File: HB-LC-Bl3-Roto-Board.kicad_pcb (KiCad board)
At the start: 2 copper layers, 43 parts, among them IC1 ArduinoProMini, J1 Taster Verdunklung, J2 Taster Fenster, J3 Taster Sonnenschutz, J4 230V, J5 24V, J6 Motor Fenster 24V, J7 Motor Sonnenschutz 230V, J8 Motor Verdunklung 24V, K1 G6S-2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

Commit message: Intermediate commit
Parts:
- moved RL2 37.3 mm to (91.3, 87.7), turned to 270 degrees
- moved RL4 1.28 mm to (63.9, 117.7)
- moved F1 0.76 mm to (100.5, 117.4)
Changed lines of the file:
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@@
   )
   (module relay:FIN4061 (layer F.Cu)
-    (at 62.75 117.05)
+    (at 63.85 117.7)
     (fp_text reference RL4 (at 4.9 2.3) (layer F.SilkS)
       (effects (font (size 1 1) (thickness 0.15)))
@@
   )
   (module relay:FIN4061 (layer F.Cu)
-    (at 57.85 104.05)
-    (fp_text reference RL2 (at 4.9 2.3) (layer F.SilkS)
+    (at 91.35 87.65 270)
+    (fp_text reference RL2 (at 4.9 2.3 90) (layer F.SilkS)
       (effects (font (size 1 1) (thickness 0.15)))
     )
-    (fp_text value FINDER-40.61 (at 7.9 4.2) (layer F.Fab)
+    (fp_text value FINDER-40.61 (at 7.9 4.2 90) (layer F.Fab)
       (effects (font (size 1 1) (thickness 0.15)))
     )
@@
     (fp_line (start 26 10) (end -3 10) (layer F.SilkS) (width 0.15))
     (fp_line (start -3 -2.5) (end 26 -2.5) (layer F.SilkS) (width 0.15))
-    (pad A1 thru_hole circle (at 0 0) (size 3 3) (drill 1.5) (layers *.Cu *.Mask)
+    (pad A1 thru_hole circle (at 0 0 270) (size 3 3) (drill 1.5) (layers *.Cu *.Mask)
       (net 4 +24V))
-    (pad A2 thru_hole circle (at 0 7.5) (size 3 3) (drill 1.5) (layers *.Cu *.Mask)
+    (pad A2 thru_hole circle (at 0 7.5 270) (size 3 3) (drill 1.5) (layers *.Cu *.Mask)
       (net 6 "Net-(D3-Pad2)"))
-    (pad 11 thru_hole rect (at 20 0) (size 2.5 4) (drill 1.5) (layers *.Cu *.Mask)
+    (pad 11 thru_hole rect (at 20 0 270) (size 2.5 4) (drill 1.5) (layers *.Cu *.Mask)
       (net 52 /L_FUSED))
-    (pad 14 thru_hole rect (at 25 0) (size 2.5 4) (drill 1.5) (layers *.Cu *.Mask)
+    (pad 14 thru_hole rect (at 25 0 270) (size 2.5 4) (drill 1.5) (layers *.Cu *.Mask)
       (net 49 /M2_L))
-    (pad 12 thru_hole rect (at 15 0) (size 2.5 4) (drill 1.5) (layers *.Cu *.Mask)
+    (pad 12 thru_hole rect (at 15 0 270) (size 2.5 4) (drill 1.5) (layers *.Cu *.Mask)
       (net 50 "Net-(RL2-Pad12)"))
-    (pad 22 thru_hole rect (at 15 7.5) (size 2.5 4) (drill 1.5) (layers *.Cu *.Mask)
+    (pad 22 thru_hole rect (at 15 7.5 270) (size 2.5 4) (drill 1.5) (layers *.Cu *.Mask)
       (net 50 "Net-(RL2-Pad12)"))
-    (pad 21 thru_hole rect (at 20 7.5) (size 2.5 4) (drill 1.5) (layers *.Cu *.Mask)
+    (pad 21 thru_hole rect (at 20 7.5 270) (size 2.5 4) (drill 1.5) (layers *.Cu *.Mask)
       (net 52 /L_FUSED))
-    (pad 24 thru_hole rect (at 25 7.5) (size 2.5 4) (drill 1.5) (layers *.Cu *.Mask)
+    (pad 24 thru_hole rect (at 25 7.5 270) (size 2.5 4) (drill 1.5) (layers *.Cu *.Mask)
       (net 49 /M2_L))
   )
@@
   )
   (module Fuse:Fuseholder_Cylinder-5x20mm_Schurter_FPG4_Vertical_Closed (layer F.Cu)
-    (at 100.15 118.1 270)
+    (at 100.45 117.4 270)
     (descr "Shock-Safe Fuseholder, 5 x 20 mm, Slotted Cap/Fingergrip, vertical, IEC 60335-1; 250VAC/10A VDE; 500V/16A UL/CSA (https://us.schurter.com/bundles/snceschurter/epim/_ProdPool_/newDS/en/typ_FPG4.pdf)")
     (tags "fuse holder vertical 5x20mm")

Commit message: Version 1
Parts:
- added C10: 100n, Capacitor_THT:C_Rect_L4.6mm_W3.0mm_P2.50mm_MKS02_FKP02, F.Cu at (92.8, 113.4)
- added C7: 100n, Capacitor_THT:C_Rect_L4.6mm_W3.0mm_P2.50mm_MKS02_FKP02, F.Cu at (104.2, 113.6)
- added C8: 100n, Capacitor_THT:C_Rect_L4.6mm_W3.0mm_P2.50mm_MKS02_FKP02, F.Cu at (115.6, 113.6)
- added C9: 100n, Capacitor_THT:C_Rect_L4.6mm_W3.0mm_P2.50mm_MKS02_FKP02, F.Cu at (100.6, 113.4)
- added H1: MountingHole, MountingHole:MountingHole_3.2mm_M3, F.Cu at (79.2, 132.0)
- added H2: MountingHole, MountingHole:MountingHole_3.2mm_M3, F.Cu at (121.2, 85.6)
- added H3: MountingHole, MountingHole:MountingHole_3.2mm_M3, F.Cu at (29.8, 87.2)
- added R10: 47, Resistor_THT:R_Axial_DIN0204_L3.6mm_D1.6mm_P5.08mm_Horizontal, F.Cu at (123.6, 116.4)
- added R11: 10k, Resistor_THT:R_Axial_DIN0204_L3.6mm_D1.6mm_P5.08mm_Horizontal, F.Cu at (106.6, 116.4)
- added R12: 10k, Resistor_THT:R_Axial_DIN0204_L3.6mm_D1.6mm_P5.08mm_Horizontal, F.Cu at (118.0, 116.4)
- added R13: 47, Resistor_THT:R_Axial_DIN0204_L3.6mm_D1.6mm_P5.08mm_Horizontal, F.Cu at (104.0, 116.4)
- added R14: 47, Resistor_THT:R_Axial_DIN0204_L3.6mm_D1.6mm_P5.08mm_Horizontal, F.Cu at (115.4, 116.4)
- added R15: 10k, Resistor_THT:R_Axial_DIN0204_L3.6mm_D1.6mm_P5.08mm_Horizontal, F.Cu at (98.2, 116.3)
- added R16: 47, Resistor_THT:R_Axial_DIN0204_L3.6mm_D1.6mm_P5.08mm_Horizontal, F.Cu at (100.8, 116.3)
- added R17: 10k, Resistor_THT:R_Axial_DIN0204_L3.6mm_D1.6mm_P5.08mm_Horizontal, F.Cu at (95.2, 116.3)
- added R18: 47, Resistor_THT:R_Axial_DIN0204_L3.6mm_D1.6mm_P5.08mm_Horizontal, F.Cu at (92.6, 116.3)
- added R7: 10k, Resistor_THT:R_Axial_DIN0204_L3.6mm_D1.6mm_P5.08mm_Horizontal, F.Cu at (109.6, 116.4)
- added R8: 10k, Resistor_THT:R_Axial_DIN0204_L3.6mm_D1.6mm_P5.08mm_Horizontal, F.Cu at (121.0, 116.4)
- added R9: 47, Resistor_THT:R_Axial_DIN0204_L3.6mm_D1.6mm_P5.08mm_Horizontal, F.Cu at (112.2, 116.4)
- C1: value 10µF Tantal -> 10µF
- C4, C5: value 100n -> 1u; footprint Capacitor_THT:C_Rect_L4.6mm_W3.0mm_P2.50mm_MKS02_FKP02 -> Capacitor_THT:C_Rect_L7.2mm_W5.5mm_P5.00mm_FKS2_FKP2_MKS2_MKP2
- J1, J2, J3: footprint TerminalBlock_WAGO:TerminalBlock_WAGO_250-403_1x03_P2.50mm_45Degree -> wago:P-250-403
- Q1, Q2, Q5, Q6: value BC817 -> BC337
- R1, R2, R3, R6: value 2k7 -> 7k5
- R4, R5: value 10k -> 2k4
- moved C1 130.4 mm to (33.8, 70.8)
- moved C2 105.9 mm to (40.0, 72.6)
- moved J3 104.0 mm to (104.4, 129.0), turned to 90 degrees
- moved D4 103.7 mm to (77.4, 120.6), turned to 90 degrees
- moved U1 99.1 mm to (43.8, 75.8), turned to 180 degrees
- moved R5 96.4 mm to (85.4, 112.0), turned to 180 degrees
- moved J1 92.4 mm to (93.0, 129.0), turned to 90 degrees
- moved Q5 81.6 mm to (85.8, 54.4), turned to 180 degrees
- moved R1 78.0 mm to (82.8, 70.0), turned to 180 degrees
- moved C4 74.3 mm to (41.6, 63.2), turned to 270 degrees
- moved K4 72.7 mm to (94.2, 46.8), turned to 90 degrees
- moved Q6 72.6 mm to (87.8, 43.4), turned to 180 degrees
- moved C5 72.4 mm to (37.0, 62.6), turned to 180 degrees
- moved J4 70.5 mm to (29.2, 130.5), turned to 0 degrees
- moved C3 70.2 mm to (112.0, 113.6), turned to 180 degrees
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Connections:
- C3 pad 1: +3V3 -> /TA3
- C6 pad 1: GND -> /TA1
- C6 pad 2: +3V3 -> GND
- IC1 pad 10: /TA5 -> /M3_EN
- IC1 pad 12: /TA6 -> /M3_DIR
- IC1 pad 17: /M1_DIR -> /TA3
- IC1 pad 18: /M1_EN -> /TA4
- IC1 pad 19: /M2_EN -> /TA5
- IC1 pad 20: /M2_DIR -> /M2_EN
- IC1 pad 25: /M3_DIR -> /TA6
- IC1 pad 26: /M3_EN -> /M2_DIR
- IC1 pad 8: /TA4 -> /M1_DIR
- IC1 pad 9: /TA3 -> /M1_EN
- J4 pad 1: /N -> /L
- J4 pad 2: /L -> /N
- J5 pad L1: GND -> +24V
- J5 pad L2: +24V -> GND
- J7 pad 2: /M2_L1 -> /M2_L2
- J7 pad 3: /M2_L2 -> /M2_L1
- J8 pad L1: /M3_B -> /M3_A
- J8 pad L2: /M3_A -> /M3_B
- K1 pad 5: Net-(K1-Pad5) -> +24V
- K1 pad 8: +24V -> Net-(K1-Pad8)
- K2 pad 10: GND -> Net-(K1-Pad4)
- K2 pad 3: Net-(K1-Pad9) -> GND
- K2 pad 4: /M1_A -> /M1_B
- K2 pad 5: GND -> Net-(K1-Pad4)
- K2 pad 8: Net-(K1-Pad9) -> GND
- K2 pad 9: /M1_B -> /M1_A
- RL2 pad 11: /L_FUSED -> /M2_L
- RL2 pad 14: /M2_L -> /L_FUSED
- RL2 pad 21: /L_FUSED -> /M2_L
- RL2 pad 24: /M2_L -> /L_FUSED
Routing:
- net GND: track 0.00 -> 502.4 mm, vias 0 -> 7
- net +24V: track 0.00 -> 252.5 mm, vias 0 -> 2
- net +3V3: track 0.00 -> 220.6 mm, vias 0 -> 10
- net /TA3: track 0.00 -> 115.5 mm, vias 0 -> 2
- net /TA1: track 0.00 -> 108.8 mm, vias 0 -> 2
- net /TA4: track 0.00 -> 105.3 mm, vias 0 -> 2
- net /TA2: track 0.00 -> 100.5 mm, vias 0 -> 2
- net /TA5: track 0.00 -> 100.1 mm, vias 0 -> 2
- net /TA6: track 0.00 -> 87.1 mm, vias 0 -> 2
- net /M2_DIR: track 0.00 -> 80.6 mm, vias 0 -> 2
- net /M2_EN: track 0.00 -> 69.3 mm, vias 0 -> 1
- net /RF_INT: track 0.00 -> 43.4 mm, vias 0 -> 2
- net /M1_DIR: track 0.00 -> 38.3 mm, vias 0 -> 2
- net /M1_EN: track 0.00 -> 31.3 mm, vias 0 -> 2
- net /L_FUSED: track 0.00 -> 25.4 mm
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- added copper zone on B.Cu, net GND
- added copper zone on F.Cu, net GND
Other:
- board outline added: 100 x 100 mm
- net class 230V added: clearance 2.5, trace_width 2, via_dia 3, via_drill 1.5
- net class Default: clearance 0.2 -> 0.6; trace_width 0.25 -> 0.4; via_dia 0.8 -> 1.2; via_drill 0.4 -> 0.8
- net class le24v_supply added: clearance 0.6, trace_width 0.8, via_dia 1.5, via_drill 1
- rule trace_clearance: 0.2 -> 0.6
- board text added: "(C) Creative Commons"
- board text added: "+24V GND"
- board text added: "230V Anschluss und 230V Motor"
- board text added: "24V Anschluss und 24V Motoren"
- board text added: "Fenster"
- board text added: "HB-LC-Bl3-Roto"
- board text added: "L"
- board text added: "L1"
- board text added: "L2"
- board text added: "N"
- board text added: "Sonnenschutz"
- board text added: "Taster"
- board text added: "V1.0"
- board text added: "Verdunklung"

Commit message: Fixed rotated connector, improved pcb print
- J6, J5 and J8 are 180° rotated. Still ok to assemble. But some prints
are no longer readable. Fixed
- Print of resistor array for R7..R18 is partly wrong. Corrected. Only a
PCB print issue
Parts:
- moved J8 6.10 mm to (116.4, 41.3), turned to 0 degrees
- moved J5 6.01 mm to (116.3, 52.0), turned to 0 degrees
- moved J6 5.50 mm to (115.8, 73.9), turned to 0 degrees
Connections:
- J5 pad L1: +24V -> GND
- J5 pad L2: GND -> +24V
- J6 pad L1: /M1_B -> /M1_A
- J6 pad L2: /M1_A -> /M1_B
- J8 pad L1: /M3_A -> /M3_B
- J8 pad L2: /M3_B -> /M3_A
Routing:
- net +24V: track 252.5 -> 247.1 mm
- net /M1_A: track 21.9 -> 19.0 mm
- net /M3_B: track 22.3 -> 19.5 mm
- net /M1_B: track 14.9 -> 14.1 mm

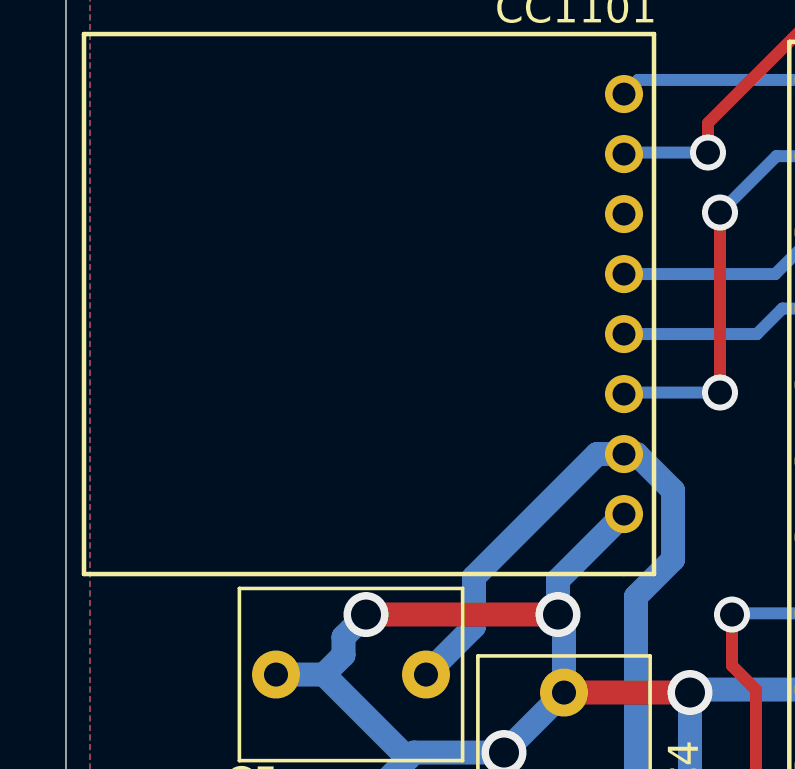
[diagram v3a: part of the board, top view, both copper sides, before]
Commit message: Added missing GND connections for CC1101
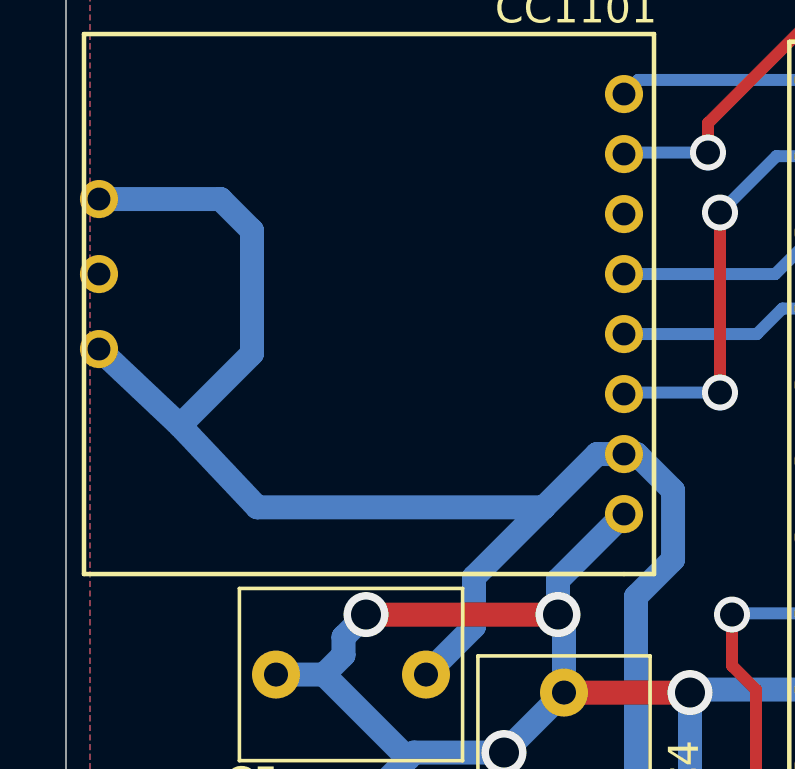
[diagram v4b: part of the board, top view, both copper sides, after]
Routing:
- net GND: track 502.6 -> 532.6 mm
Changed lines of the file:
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@@
-(kicad_pcb (version 20171130) (host pcbnew 5.1.5-52549c5~84~ubuntu18.04.1)
+(kicad_pcb (version 20171130) (host pcbnew 5.1.5-52549c5~86~ubuntu18.04.1)
   (general
     (thickness 1.6)
     (drawings 39)
-    (tracks 614)
+    (tracks 622)
     (zones 0)
     (modules 62)
-    (nets 69)
+    (nets 70)
   )
   (page A4)
@@
   (net 67 /TA4_IN)
   (net 68 "Net-(K1-Pad8)")
+  (net 69 "Net-(U3-Pad9)")
   (net_class Default "This is the default net class."
     (clearance 0.6)
@@
     (add_net "Net-(RL2-Pad12)")
     (add_net "Net-(U3-Pad6)")
+    (add_net "Net-(U3-Pad9)")
   )
   (net_class 230V ""
@@
     (add_net "Net-(K3-Pad9)")
   )
+  (module radio:CC1101_Module (layer F.Cu)
+    (at 43.6 50.25 90)
+    (fp_text reference U3 (at 0 -4.5 90) (layer F.SilkS) hide
+      (effects (font (size 1 1) (thickness 0.15)))
+    )
+    (fp_text value CC1101-868MHz-Module (at 0 -6.27 90) (layer F.Fab)
+      (effects (font (size 1 1) (thickness 0.15)))
+    )
+    (fp_line (start -9 1) (end -9 0) (layer F.SilkS) (width 0.15))
+    (fp_line (start 9 1) (end -9 1) (layer F.SilkS) (width 0.15))
+    (fp_line (start 9 -18) (end 9 1) (layer F.SilkS) (width 0.15))
+    (fp_line (start -9 -18) (end 9 -18) (layer F.SilkS) (width 0.15))
+    (fp_line (start -9 0) (end -9 -18) (layer F.SilkS) (width 0.15))
+    (fp_text user CC1101 (at 9.85 -1.6 180) (layer F.SilkS)
+      (effects (font (size 1 1) (thickness 0.15)))
+    )
+    (pad 8 thru_hole circle (at 7 0 90) (size 1.27 1.27) (drill 0.762) (layers *.Cu *.Mask)
+      (net 23 /RF_CSN))
+    (pad 7 thru_hole circle (at 5 0 90) (size 1.27 1.27) (drill 0.762) (layers *.Cu *.Mask)
+      (net 31 /RF_INT))
+    (pad 6 thru_hole circle (at 3 0 90) (size 1.27 1.27) (drill 0.762) (layers *.Cu *.Mask)
+      (net 51 "Net-(U3-Pad6)"))
+    (pad 5 thru_hole circle (at 1 0 90) (size 1.27 1.27) (drill 0.762) (layers *.Cu *.Mask)
+      (net 21 /RF_MISO))
+    (pad 4 thru_hole circle (at -1 0 90) (size 1.27 1.27) (drill 0.762) (layers *.Cu *.Mask)
+      (net 20 /RF_SCLK))
+    (pad 3 thru_hole circle (at -3 0 90) (size 1.27 1.27) (drill 0.762) (layers *.Cu *.Mask)
+      (net 22 /RF_MOSI))
+    (pad 2 thru_hole circle (at -5 0 90) (size 1.27 1.27) (drill 0.762) (layers *.Cu *.Mask)
+      (net 1 GND))
+    (pad 1 thru_hole circle (at -7 0 90) (size 1.27 1.27) (drill 0.762) (layers *.Cu *.Mask)
+      (net 2 +3V3))
+    (pad 10 thru_hole circle (at -1.5 -17.5 90) (size 1.27 1.27) (drill 0.762) (layers *.Cu *.Mask)
+      (net 1 GND))
+    (pad 9 thru_hole circle (at 1 -17.5 90) (size 1.27 1.27) (drill 0.762) (layers *.Cu *.Mask)
+      (net 69 "Net-(U3-Pad9)"))
+    (pad 11 thru_hole circle (at 3.5 -17.5 90) (size 1.27 1.27) (drill 0.762) (layers *.Cu *.Mask)
+      (net 1 GND))
+  )
   (module MountingHole:MountingHole_3.2mm_M3 (layer F.Cu)
     (at 29.8 87.2)
@@
     )
   )
-  (module radio:CC1101_Module (layer F.Cu)
-    (at 43.6 50.25 90)
-    (fp_text reference U3 (at 0 -4.5 90) (layer F.SilkS) hide
-      (effects (font (size 1 1) (thickness 0.15)))
-    )
-    (fp_text value CC1101-868MHz-Module (at 0 -6.27 90) (layer F.Fab)
-      (effects (font (size 1 1) (thickness 0.15)))
-    )
-    (fp_line (start -9 1) (end -9 0) (layer F.SilkS) (width 0.15))
-    (fp_line (start 9 1) (end -9 1) (layer F.SilkS) (width 0.15))
-    (fp_line (start 9 -18) (end 9 1) (layer F.SilkS) (width 0.15))
-    (fp_line (start -9 -18) (end 9 -18) (layer F.SilkS) (width 0.15))
-    (fp_line (start -9 0) (end -9 -18) (layer F.SilkS) (width 0.15))
-    (fp_text user CC1101 (at 9.85 -1.6) (layer F.SilkS)
-      (effects (font (size 1 1) (thickness 0.15)))
-    )
-    (pad 8 thru_hole circle (at 7 0 90) (size 1.27 1.27) (drill 0.762) (layers *.Cu *.Mask)
-      (net 23 /RF_CSN))
-    (pad 7 thru_hole circle (at 5 0 90) (size 1.27 1.27) (drill 0.762) (layers *.Cu *.Mask)
-      (net 31 /RF_INT))
-    (pad 6 thru_hole circle (at 3 0 90) (size 1.27 1.27) (drill 0.762) (layers *.Cu *.Mask)
-      (net 51 "Net-(U3-Pad6)"))
-    (pad 5 thru_hole circle (at 1 0 90) (size 1.27 1.27) (drill 0.762) (layers *.Cu *.Mask)
-      (net 21 /RF_MISO))
-    (pad 4 thru_hole circle (at -1 0 90) (size 1.27 1.27) (drill 0.762) (layers *.Cu *.Mask)
-      (net 20 /RF_SCLK))
-    (pad 3 thru_hole circle (at -3 0 90) (size 1.27 1.27) (drill 0.762) (layers *.Cu *.Mask)
-      (net 22 /RF_MOSI))
-    (pad 2 thru_hole circle (at -5 0 90) (size 1.27 1.27) (drill 0.762) (layers *.Cu *.Mask)
-      (net 1 GND))
-    (pad 1 thru_hole circle (at -7 0 90) (size 1.27 1.27) (drill 0.762) (layers *.Cu *.Mask)
-      (net 2 +3V3))
-  )
   (module supply:SIL-4 (layer F.Cu)
     (at 43.8 75.8 180)
@@
   (segment (start 44.019802 55.25) (end 45.235001 56.465199) (width 0.8) (layer B.Cu) (net 1))
   (segment (start 43.6 55.25) (end 44.019802 55.25) (width 0.8) (layer B.Cu) (net 1))
-  (segment (start 42.701975 55.25) (end 38.6 59.351975) (width 0.8) (layer B.Cu) (net 1))
   (segment (start 43.6 55.25) (end 42.701975 55.25) (width 0.8) (layer B.Cu) (net 1))
   (segment (start 43.2 71.9) (end 42.5 72.6) (width 0.8) (layer B.Cu) (net 1))
@@
   (segment (start 117.6 54.5995) (end 120.5 57.4995) (width 0.8) (layer B.Cu) (net 1))
   (segment (start 117.6 52.9745) (end 117.6 54.5995) (width 0.8) (layer B.Cu) (net 1))
+  (segment (start 40.925987 57.025987) (end 31.375987 57.025987) (width 0.8) (layer B.Cu) (net 1))
+  (segment (start 40.925987 57.025987) (end 38.6 59.351975) (width 0.8) (layer B.Cu) (net 1))
+  (segment (start 42.701975 55.25) (end 40.925987 57.025987) (width 0.8) (layer B.Cu) (net 1))
+  (segment (start 26.1 46.75) (end 30.15 46.75) (width 0.8) (layer B.Cu) (net 1))
+  (segment (start 30.15 46.75) (end 31.2 47.8) (width 0.8) (layer B.Cu) (net 1))
+  (segment (start 31.2 51.9) (end 28.8 54.3) (width 0.8) (layer B.Cu) (net 1))
+  (segment (start 31.2 47.8) (end 31.2 51.9) (width 0.8) (layer B.Cu) (net 1))
+  (segment (start 31.375987 57.025987) (end 28.8 54.3) (width 0.8) (layer B.Cu) (net 1))
+  (segment (start 28.8 54.3) (end 26.1 51.75) (width 0.8) (layer B.Cu) (net 1))
   (via (at 48.6 77.6) (size 1.5) (drill 1) (layers F.Cu B.Cu) (net 2))
   (via (at 45 81.2) (size 1.5) (drill 1) (layers F.Cu B.Cu) (net 2))
